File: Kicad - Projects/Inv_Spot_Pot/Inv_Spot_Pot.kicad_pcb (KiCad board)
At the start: 2 copper layers, 190 x 179.5 mm, 111 parts, among them J2 PWM, J3 Display_Power, J4 24V, J5 24V, J6 PWM, K1 Y14x-1C-xxDS, Q1 60N60, Q2 60N60, Q3 60N60, Q4 60N60, T1 Transformer_1P_2S, U2 LTV-817S

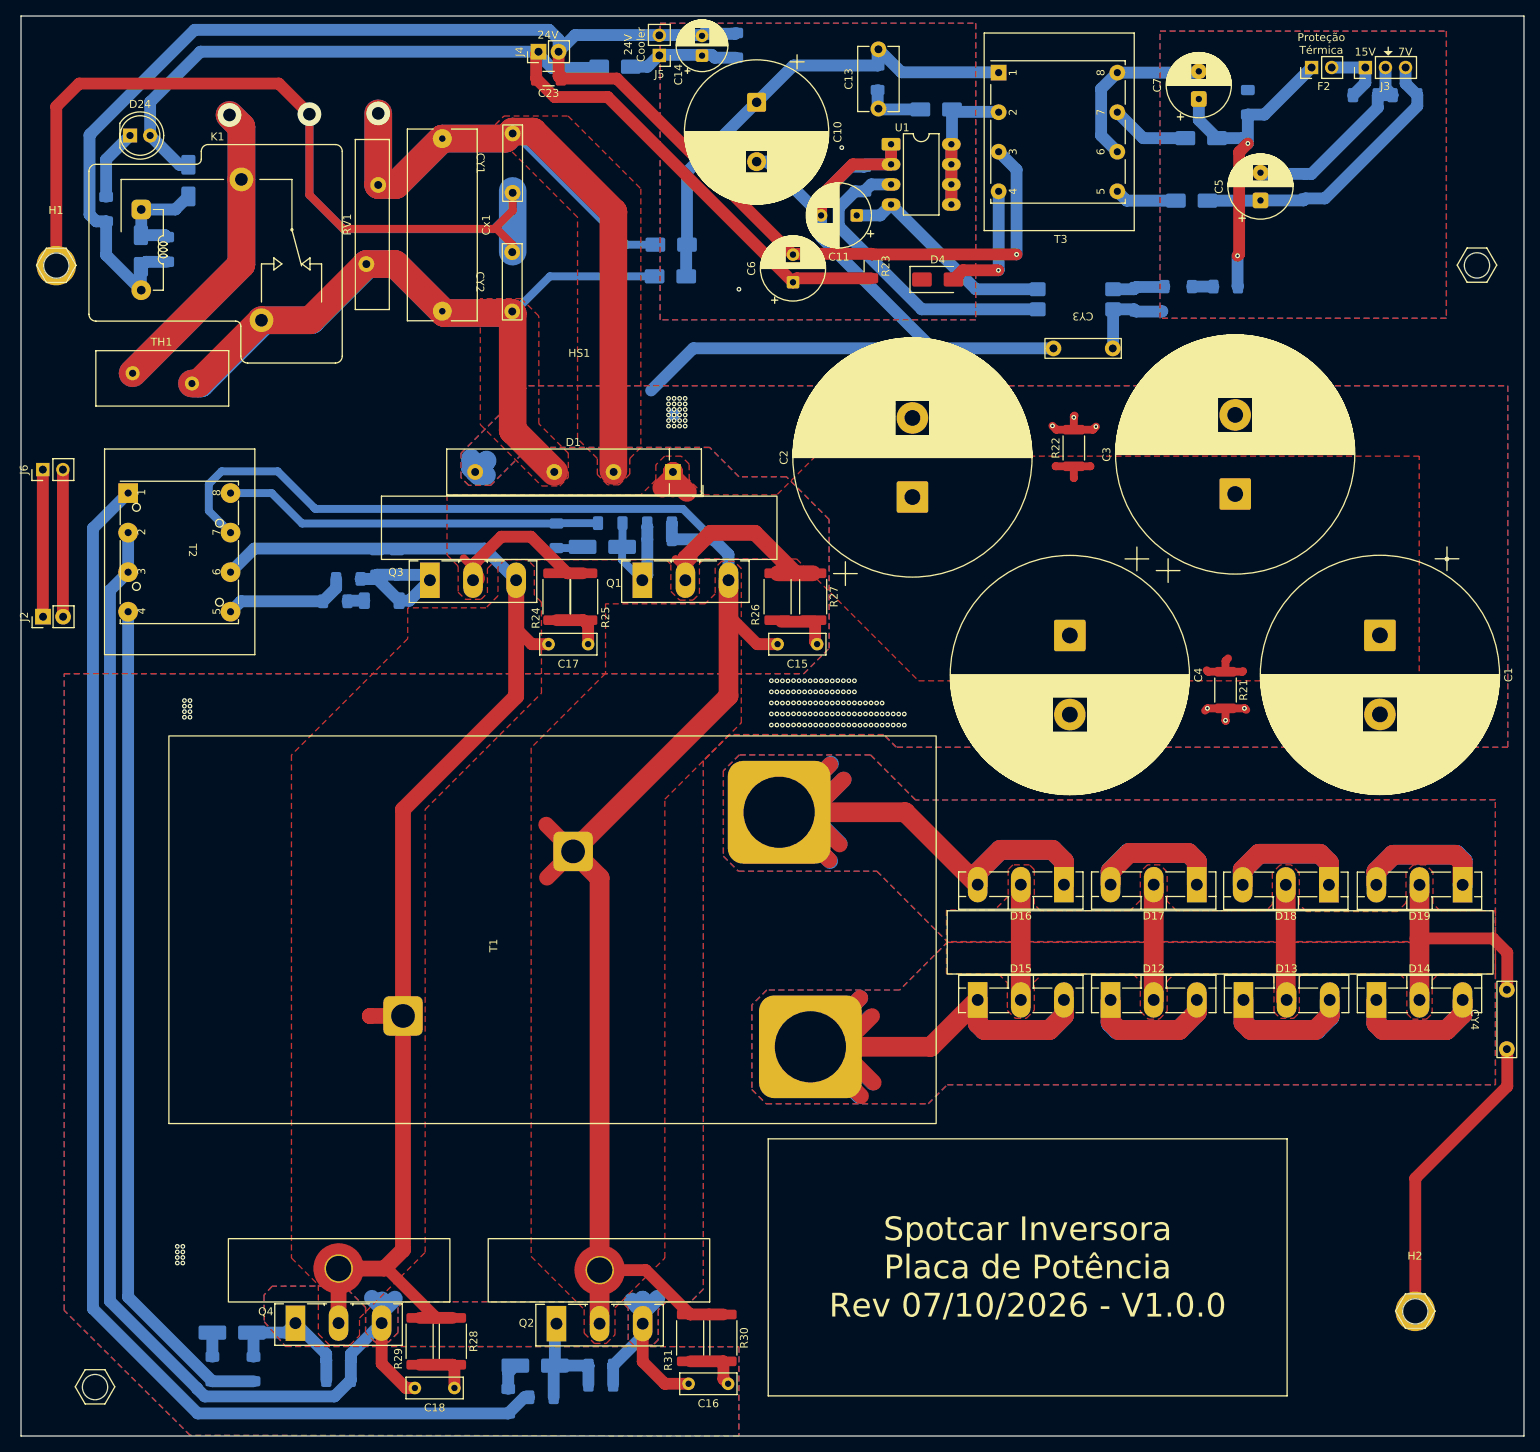
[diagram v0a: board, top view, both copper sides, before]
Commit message: Finalização - Placa Protótipo
Versão final da placa protótipo - placa já validada

Alterações:
 - Melhoras no plano terra para retorno de potência
 - Blindagem das trilhas de PWM para os IGBTs inferiores
 - Alargamento das trilhas de saída para a retificação

Falta:
 - Colocar todos os SMDs no lado TOP da placa
 - Ajustar posição dos IGBTs e transformador
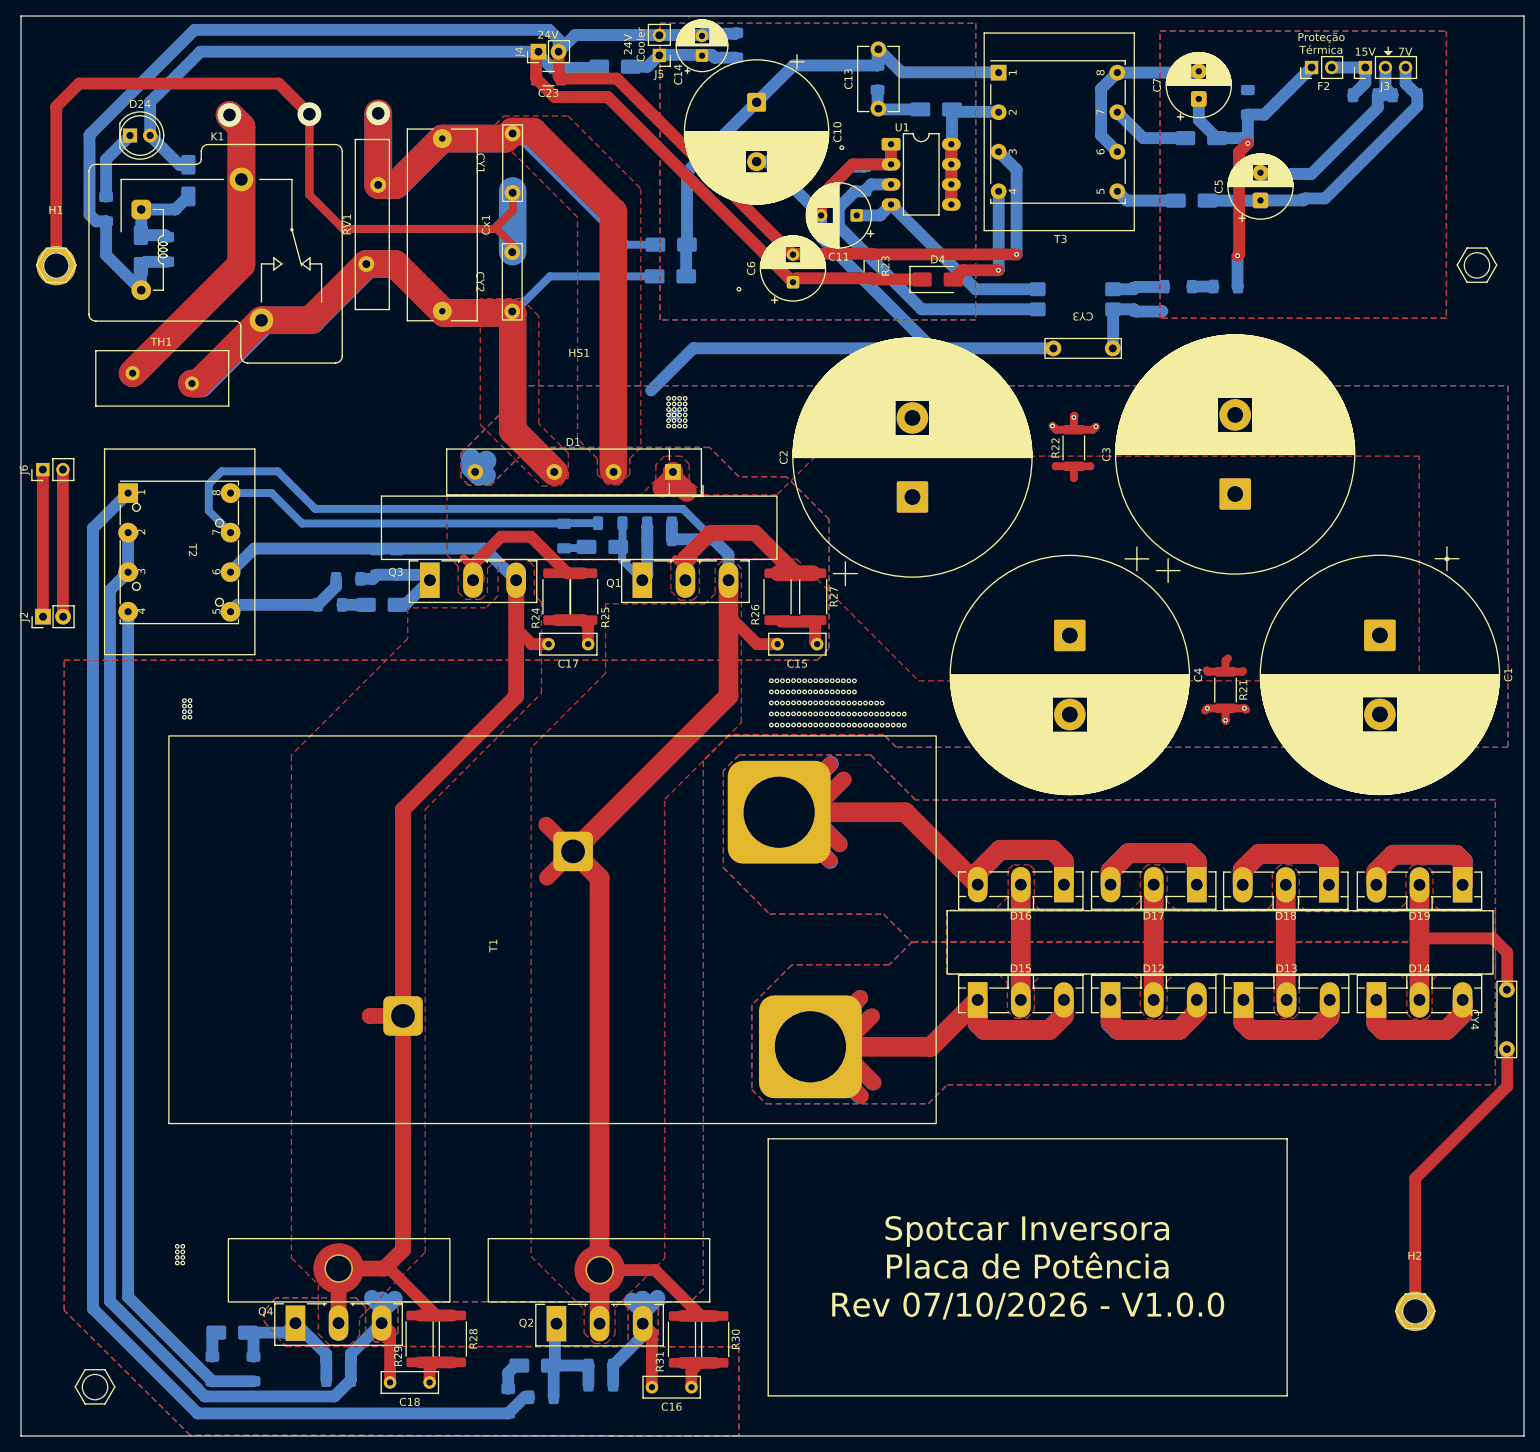
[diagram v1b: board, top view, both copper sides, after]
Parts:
- D10: footprint Diode_SMD:D_SOD-128 -> Diode_SMD:D_SMA
- D11, D8, D9: footprint Diode_SMD:D_SMA_Handsoldering -> Diode_SMD:D_SMA
- D22, D23: value 1N4007 -> M7
- R18, R2, R20, R6: value 15 -> 20
- R7: value 510 -> 2k7
- moved C16 4.65 mm to (99.4, 186.3)
- moved C18 3.21 mm to (66.3, 185.7)
- moved R30 1.05 mm to (102.4, 180.3)
- moved R31 1.05 mm to (98.2, 180.3)
- moved R5 0.97 mm to (83.3, 78.7)
- moved R17 0.81 mm to (53.7, 87.4)
- moved D10 0.53 mm to (60.2, 87.4)
- moved R28 0.30 mm to (69.2, 180.2)
- moved R29 0.30 mm to (65.0, 180.2)
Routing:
- net 24V: track 128.1 -> 134.5 mm
- net Earth: track 334.0 -> 328.1 mm
- net T+: track 173.5 -> 179.1 mm
- net Gate1: track 20.2 -> 14.6 mm
- net T-: track 237.6 -> 239.1 mm
- net Net-(D8-K): track 3.36 -> 2.41 mm
- net Net-(D10-K): track 2.16 -> 2.99 mm

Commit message: Ajustes para Produção
Ajustes de DFM para produção da placa

Falta ainda a nova versão com todos os SMDs e PTHs na mesma camada
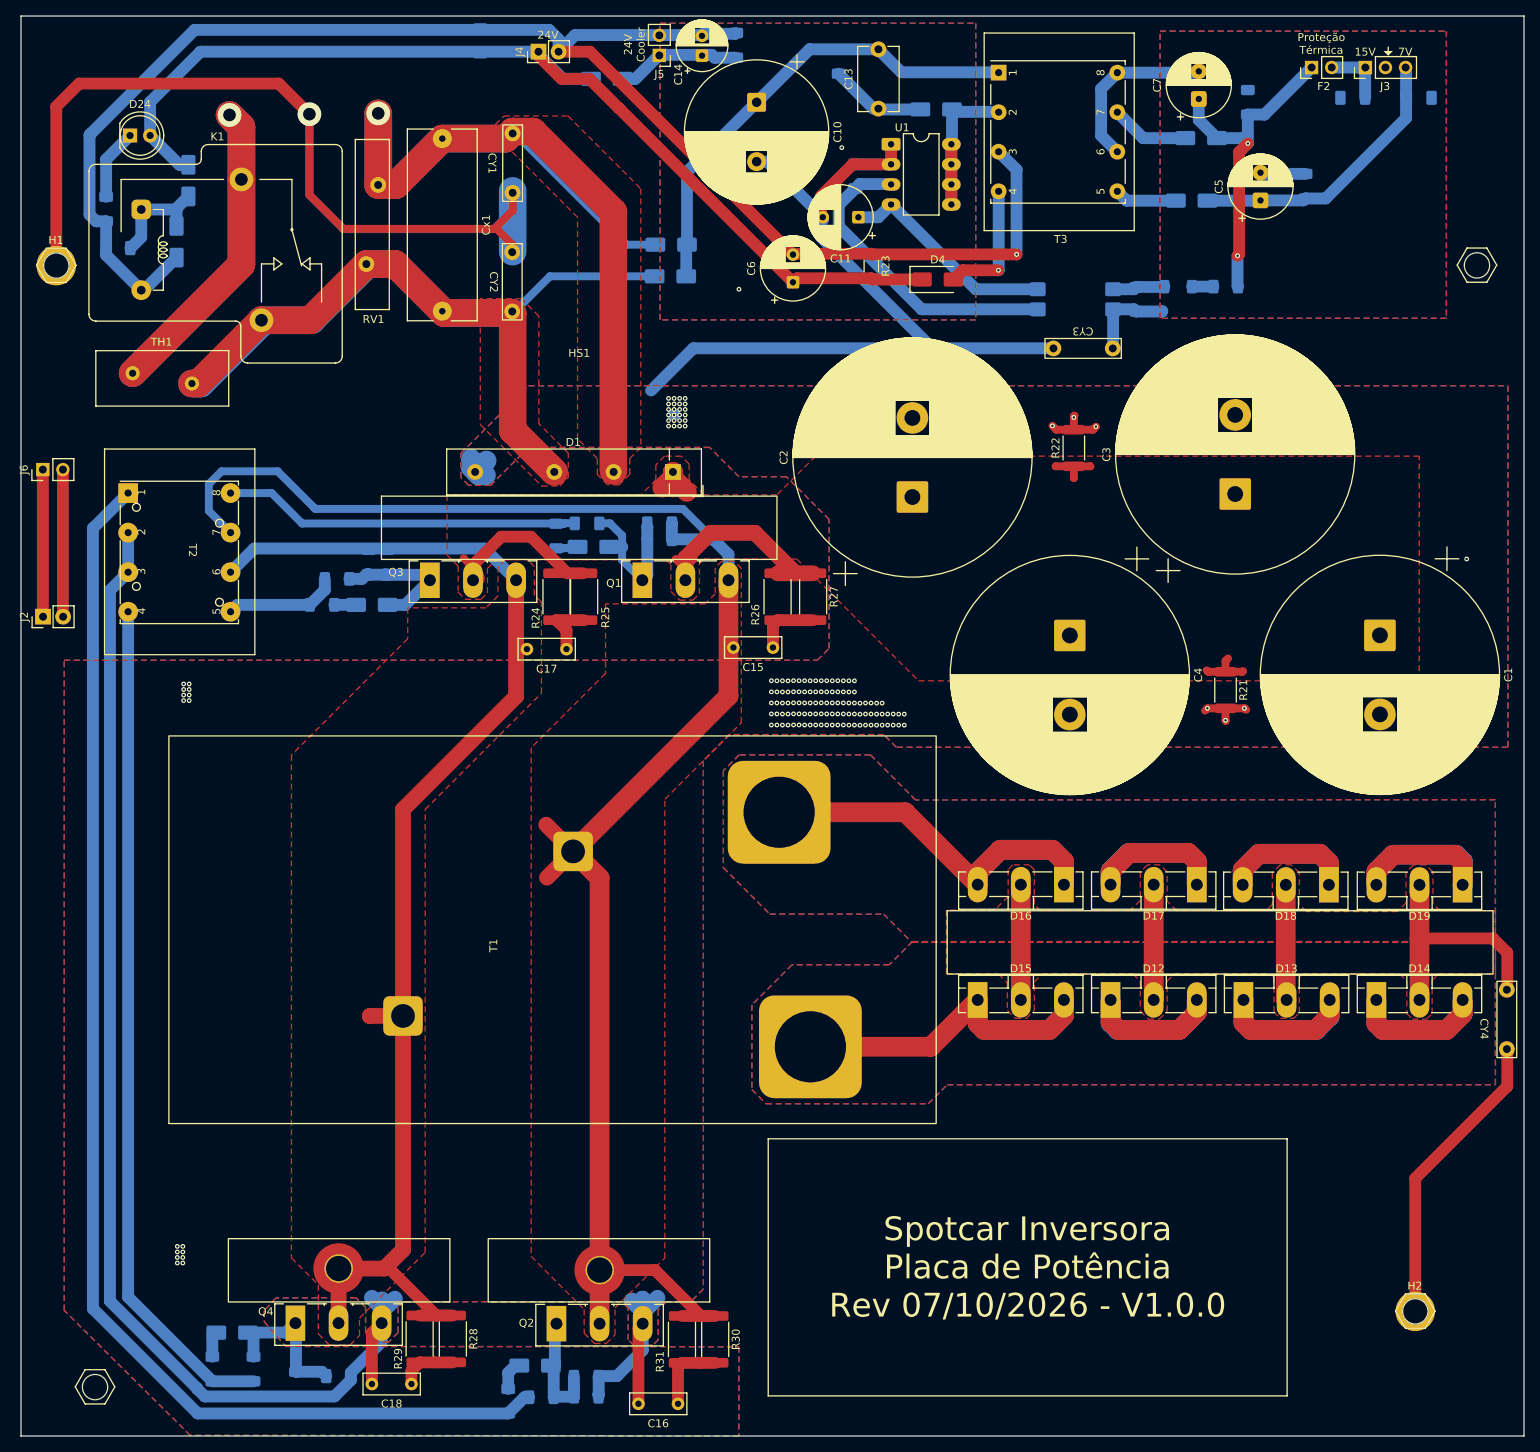
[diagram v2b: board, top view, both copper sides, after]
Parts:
- C23: moved to B.Cu
- moved C23 9.86 mm to (72.7, 16.1), turned to -90 degrees
- moved C24 6.20 mm to (26.9, 42.3), turned to 0 degrees
- moved C15 5.60 mm to (109.7, 92.8)
- moved R16 5.41 mm to (49.4, 185.9), turned to 90 degrees
- moved R12 5.35 mm to (118.0, 18.7)
- moved D22 4.65 mm to (34.3, 41.5)
- moved R4 4.34 mm to (86.1, 187.5)
- moved R6 2.93 mm to (86.2, 77.1)
- moved C17 2.80 mm to (83.6, 93.0)
- moved C16 2.70 mm to (97.7, 188.4)
- moved C18 2.31 mm to (64.0, 185.9)
- moved C19 2.07 mm to (86.1, 185.0)
- moved C21 2.00 mm to (54.8, 184.9)
- moved D25 1.85 mm to (88.7, 20.9)
- moved C8 1.84 mm to (191.4, 23.3), turned to 180 degrees
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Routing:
- net Out1: track 255.6 -> 181.9 mm
- net Out2: track 271.3 -> 201.1 mm
- net GND: track 59.1 -> 39.2 mm
- net T-: track 239.1 -> 226.9 mm
- net T+: track 179.1 -> 168.8 mm
- net Net-(D3-K): track 7.73 -> 12.2 mm
- net Gate: track 15.3 -> 18.9 mm
- net PWM: track 48.1 -> 45.2 mm
- net Gate1: track 14.6 -> 17.4 mm
- net 24V: track 134.5 -> 131.9 mm
- net Earth: track 328.1 -> 325.9 mm
- net GND_{24}: track 204.3 -> 202.2 mm
- net Net-(C16-Pad1): track 7.69 -> 9.58 mm
- net 24V-Cooler: track 14.2 -> 15.8 mm
- net ~{Gate}: track 16.1 -> 14.5 mm
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
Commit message: Alteração Menu
Correção de bugs de display no menu de corrente

Última versão da placa de potência com footprint do transformador de protótipo
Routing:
- net 310_{Aux}: track 60.2 -> 61.5 mm
- net Net-(D3-A): track 25.6 -> 26.9 mm
- net GND: track 39.2 -> 40.4 mm
- net Net-(D6-A): track 7.89 -> 9.09 mm
- net Net-(D5-A): track 9.96 -> 11.2 mm
- net Earth: track 325.9 -> 325.8 mm, vias 152 -> 160
